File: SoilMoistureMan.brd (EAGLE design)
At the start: 23.5 x 69.9 mm, 22 parts, among them Q1 BC847CSMD, Q2 BC857C, Q3 BC847CSMD, Q4 BC847CSMD, Q5 BC847CSMD

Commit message: schematic and Routing changes
schematic and Routing changes still WIP
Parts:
- added BAT2: 2032, kzh20_lithium_batterie_holder:KZH20SMD
- D1: value SS12B -> S1A-13-F
- F1: value (none) -> Resettable_Fuse
- Q2: value BC857C -> BC847CSMD; device transistor:SOT23-BEC -> transistor-npn:SOT23
- Q3: value BC847CSMD -> BC857C; device transistor-npn:SOT23 -> transistor:SOT23-BEC
- R2: device resistor:R0805 -> rcl:R0805
- R3: value 1k -> 100k; device rcl:R0805 -> resistor:R0805
- R4: value 1k -> 10k
- R5: value 100k -> 1k
- R7: value 1k -> 100k
- moved R8 80.0 mm to (23.2, 62.2), turned to 270 degrees
- moved Q5 63.3 mm to (23.2, 51.4)
- moved D1 27.8 mm to (36.2, 40.6), turned to 180 degrees
- moved R4 19.1 mm to (17.6, 47.8), turned to 270 degrees
- moved F1 18.9 mm to (30.6, 37.3)
- moved Q4 16.8 mm to (5.08, 51.4), turned to 0 degrees
- moved Q3 16.3 mm to (21.0, 45.7)
- moved R6 9.53 mm to (9.21, 66.0), turned to 90 degrees
- moved R2 6.79 mm to (9.84, 49.2), turned to 270 degrees
- moved R7 5.85 mm to (18.7, 66.0), turned to 90 degrees
- moved Q1 5.82 mm to (6.19, 45.7)
- moved R5 5.62 mm to (5.08, 62.2)
- moved R3 3.49 mm to (16.5, 43.8)
- moved R1 3.34 mm to (11.6, 44.0)
- moved Q2 2.66 mm to (14.0, 47.5)
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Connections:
- new net N$13: Q2.3, R3.1, R4.1
- net GND: now also BAT2.-, Q2.2, Q5.2; no longer Q3.2
- net N$1: now also Q3.C, R8.2; no longer Q2.C, R4.2
- net N$10: now also Q4.1, R7.1; no longer Q3.1, R6.1
- net N$11: now also Q5.3; no longer Q4.3
- net N$12: now also Q5.1, R6.1; no longer Q4.1, R5.1
- net N$2: now also R5.1; no longer R4.1
- net N$3: now also Q3.B, R4.2; no longer Q2.B, R2.1, R3.2
- net N$4: now also Q2.1, R2.1; no longer R3.1
- net N$5: now also R8.1; no longer R7.1
- net N$6: now also Q3.E, R3.2; no longer Q2.E
- net N$7: now also Q4.3; no longer Q3.3
- net VCC: now also BAT2.+
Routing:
- net SOIL_PROBE_B: track 0.00 -> 114.4 mm, vias 0 -> 3
- net SOIL_PROBE_A: track 0.00 -> 71.2 mm, vias 0 -> 1
- net GND: track 0.00 -> 59.9 mm, vias 0 -> 6
- net N$1: track 0.00 -> 45.6 mm, vias 0 -> 2
- net VCC: track 0.00 -> 37.0 mm
- net N$10: track 0.00 -> 30.9 mm, vias 0 -> 2
- net N$12: track 0.00 -> 26.8 mm
- net N$6: track 0.00 -> 21.3 mm, vias 0 -> 3
- net N$4: track 0.00 -> 15.1 mm
- net N$13: track 0.00 -> 10.0 mm
- net N$5: track 0.00 -> 9.25 mm
- net N$11: track 0.00 -> 9.07 mm
- net N$7: track 0.00 -> 7.38 mm
- net N$3: track 0.00 -> 7.05 mm
- net N$2: track 0.00 -> 4.67 mm
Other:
- outline, holes or cut-outs redrawn

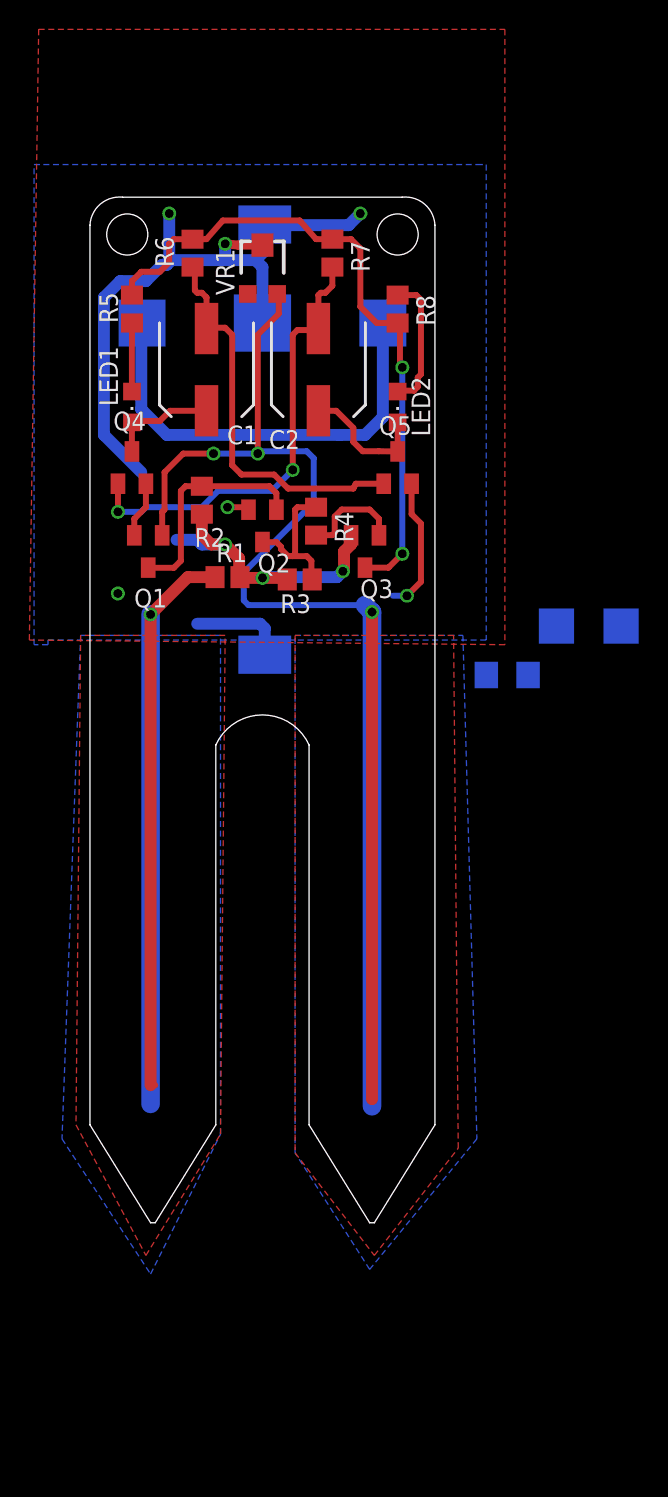
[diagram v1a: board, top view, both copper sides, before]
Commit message: Layout changes and Bat 2 changed to bat 1
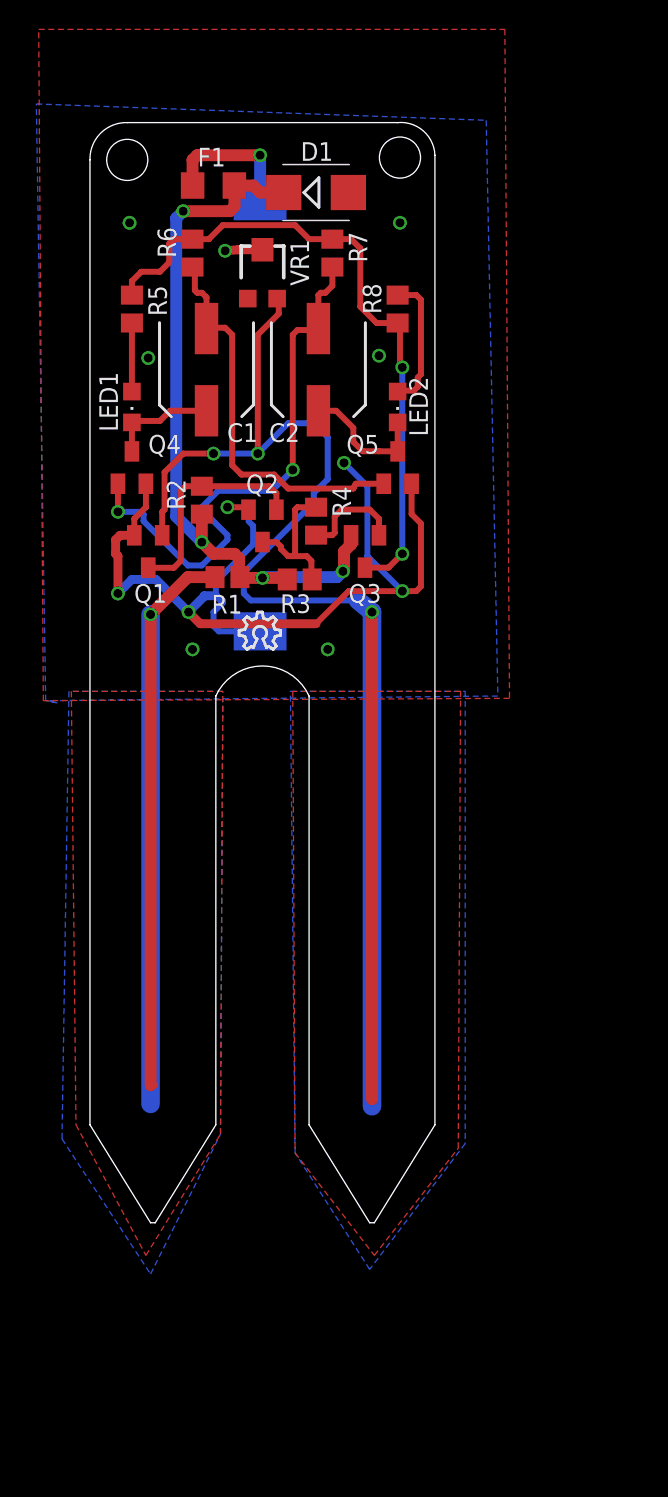
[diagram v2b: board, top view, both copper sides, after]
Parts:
- removed BAT2: 2032, kzh20_lithium_batterie_holder:KZH20SMD
- BAT1: value CR1220SMD -> 2032; device adafruit:CR1220-SMD -> kzh20_lithium_batterie_holder:KZH20SMD
- moved F1 38.9 mm to (10.6, 70.6), flipped to the top
- moved D1 34.9 mm to (17.6, 70.2), flipped to the top, turned to 0 degrees
- moved U$1 7.13 mm to (12.4, 39.1), flipped to the top
- moved BAT1 6.35 mm to (13.8, 54.9), turned to 90 degrees
- moved VR1 0.32 mm to (14.0, 64.8)
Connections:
- net GND: no longer BAT2.-
- net VCC: now also BAT1.+; no longer BAT1.+$1, BAT1.+$2, BAT2.+
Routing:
- net N$6: track 21.3 -> 50.2 mm, vias 3 -> 4
- net VCC: track 37.0 -> 9.61 mm, vias 0 -> 1
- net GND: track 59.9 -> 68.5 mm, vias 6 -> 12
- net N$10: track 30.9 -> 38.3 mm
- net SOIL_PROBE_B: track 114.4 -> 118.1 mm
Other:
- board size 23.5 x 69.9 mm -> 23.5 x 74.9 mm

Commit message: CAD B Commit
CAD B Commit - used to produce CAD B boards
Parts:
- removed Q5: BC847CSMD, transistor-npn:SOT23
- C1: value 100uF -> 1uF; device rcl:SANYO-OSCON_SMD_C6 -> resistor:C0603
- C2: value 10uF -> 100nF; device rcl:SANYO-OSCON_SMD_C6 -> resistor:C0603
- D1: value S1A-13-F -> 0.5A SOD-323; device diode:SMB -> adafruit:SOD-323F
- F1: value Resettable_Fuse -> 100MA PTC FUSE; device adafruit:R1206 -> rcl:R0805
- LED1, LED2: value GENERIC_0805_SMD_LED -> GENERIC_0603_SMD_LED; device led:CHIPLED_0805 -> led:SML0603
- Q2: value BC847CSMD -> BC857C; device transistor-npn:SOT23 -> transistor:SOT23-BEC
- Q3: value BC857C -> BC847CSMD; device transistor:SOT23-BEC -> transistor-npn:SOT23
- R1: value 20k -> 150k; device resistor:R0805 -> resistor:R0603
- R2: value 100k -> 1Meg; device rcl:R0805 -> resistor:R0603
- R3: value 100k -> 10k; device resistor:R0805 -> resistor:R0603
- R4: value 10k -> 1Meg; device rcl:R0805 -> resistor:R0603
- R5: value 1k -> 10Meg; device rcl:R0805 -> resistor:R0603
- R6: value 100k -> 10Meg; device rcl:R0805 -> resistor:R0603
- R7: value 100k -> 2k; device rcl:R0805 -> resistor:R0603
- R8: value 1k -> 0R0; device rcl:R0805 -> resistor:R0603
- moved D1 29.1 mm to (9.05, 42.4), flipped to the bottom, turned to 270 degrees
- moved F1 29.1 mm to (13.8, 41.8), flipped to the bottom
- moved R8 19.4 mm to (13.8, 45.2), turned to 0 degrees
- moved LED2 19.2 mm to (10.3, 69.8)
- moved LED1 18.8 mm to (17.3, 69.8), turned to 0 degrees
- moved Q1 16.2 mm to (22.1, 42.5), flipped to the bottom, turned to 0 degrees
- moved R6 16.1 mm to (15.2, 51.1)
- moved Q4 15.5 mm to (19.8, 46.7), flipped to the bottom
- moved R7 14.9 mm to (18.3, 51.1), turned to 270 degrees
- moved Q3 13.6 mm to (7.46, 47.0), flipped to the bottom, turned to 0 degrees
- moved R5 13.2 mm to (12.2, 51.1)
- moved C2 13.2 mm to (19.8, 45.1), turned to 0 degrees
- moved C1 13.0 mm to (7.46, 45.4), turned to 0 degrees
- moved R3 12.6 mm to (6.19, 51.1), turned to 270 degrees
- moved R2 11.7 mm to (21.4, 51.1), turned to 90 degrees
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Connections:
- removed net N$4: Q1.3, Q2.1, R2.1
- removed net N$6: D1.C, F1.2, Q3.E, R1.2, R2.2, R3.2
- removed net SOIL_PROBE_B: Q1.1, VR1.3
- new net N$9: R1.2, VR1.2
- new net VCC_FUSED: D1.C, F1.2, Q2.E, R2.2, VR1.3
- net GND: now also Q3.2; no longer Q2.2, Q5.2, VR1.2
- net N$1: now also Q2.C, R4.2; no longer Q3.C, R8.2
- net N$10: now also C2.1, Q3.1, R6.1; no longer C2.-, Q4.1, R7.1
- net N$11: now also C2.2, LED1.C, Q4.3; no longer C2.+, Q5.3
- net N$12: now also C1.2, Q4.1, R5.1; no longer C1.-, Q5.1, R6.1
- net N$13: now also Q1.3, R2.1; no longer Q2.3, R4.1
- net N$2: now also R4.1, R8.2; no longer LED1.A, R5.1
- net N$3: now also Q2.B, R3.2; no longer Q3.B, R4.2
- net N$5: now also LED1.A, R7.1; no longer R8.1
- net N$7: now also C1.1, Q3.3, R8.1; no longer C1.+, LED1.C, Q4.3
- net SOIL_PROBE_A: now also Q1.1
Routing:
- net SOIL_PROBE_B: track 118.1 -> 0.00 mm, vias 3 -> 0
- net VCC_FUSED: track 0.00 -> 92.0 mm, vias 0 -> 1
- net N$6: track 50.2 -> 0.00 mm, vias 4 -> 0
- net SOIL_PROBE_A: track 71.2 -> 21.0 mm, vias 1 -> 4
- net N$9: track 0.00 -> 36.1 mm, vias 0 -> 3
- net N$11: track 9.07 -> 40.8 mm, vias 0 -> 4
- net N$5: track 9.25 -> 33.0 mm, vias 0 -> 4
- net N$10: track 38.3 -> 15.5 mm, vias 2 -> 1
- net GND: track 68.5 -> 91.0 mm, vias 12 -> 17
- net N$13: track 10.0 -> 29.2 mm, vias 0 -> 1
- net N$4: track 15.1 -> 0.00 mm
- net N$1: track 45.2 -> 33.3 mm
- net N$2: track 4.67 -> 13.5 mm
- net N$3: track 7.05 -> 15.5 mm, vias 0 -> 1
- net N$7: track 7.38 -> 13.6 mm, vias 0 -> 1
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- removed copper zone on layer 1, net SOIL_PROBE_B
- removed copper zone on layer 16, net SOIL_PROBE_B
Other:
- board size 23.5 x 74.9 mm -> 23.5 x 77.5 mm
- board text added: "K"

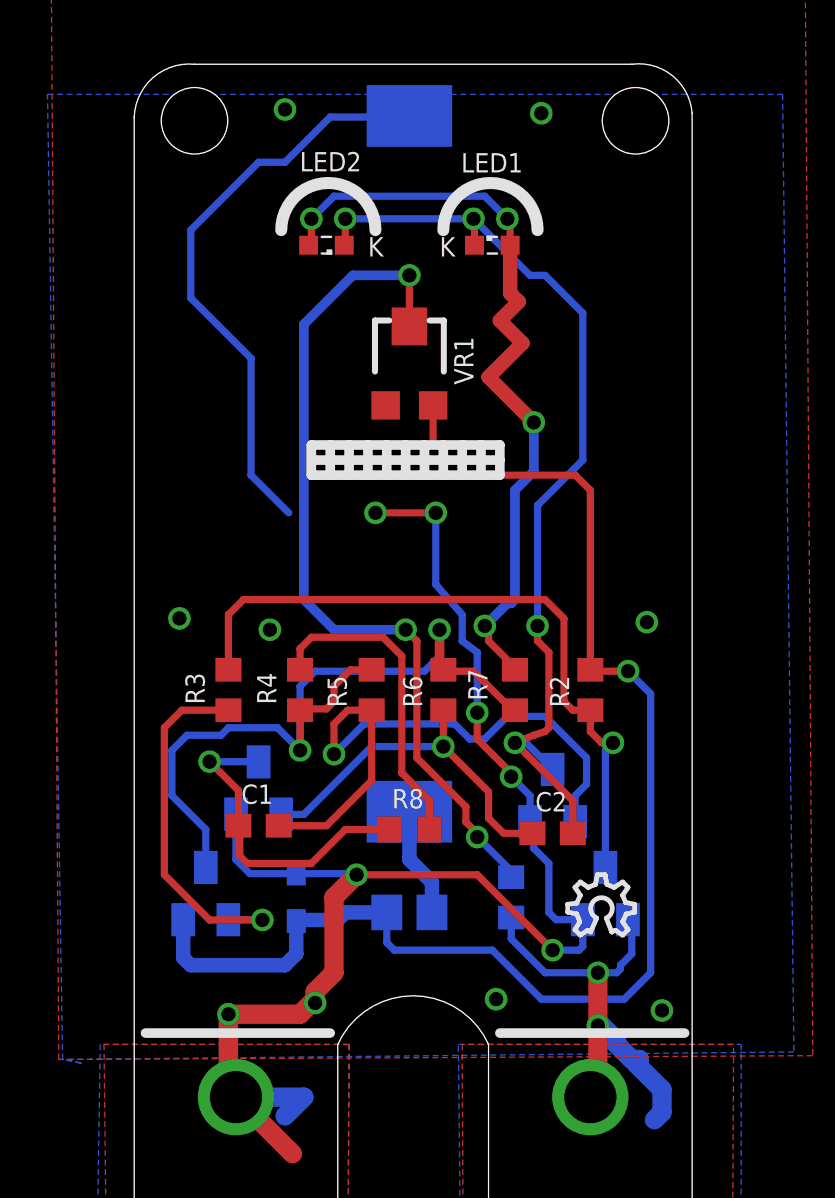
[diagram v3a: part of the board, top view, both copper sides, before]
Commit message: First CAD C commit
Updated one resistor value from 1MOhm to 100k. added warning text about
electrolysis to pcb and another to the schematic
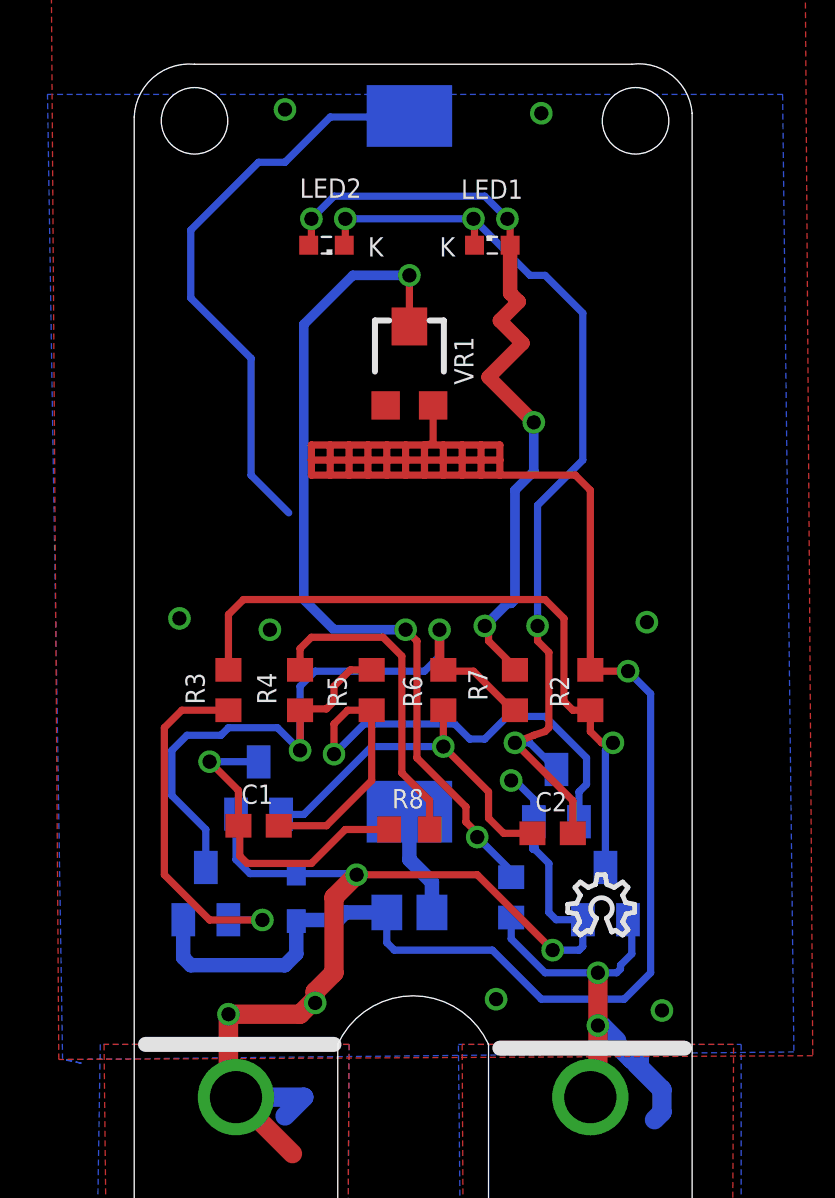
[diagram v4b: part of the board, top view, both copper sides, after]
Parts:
- Q4: value BC847CSMD -> MMBTA13LT1; device transistor-npn:SOT23 -> transistor-npn:SOT23-BEC
- R4: value 1Meg -> 100k
- moved Q4 0.16 mm to (20.0, 46.7)
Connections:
- net GND: now also Q4.E; no longer Q4.2
- net N$11: now also Q4.C; no longer Q4.3
- net N$12: now also Q4.B; no longer Q4.1
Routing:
- net GND: track 91.0 -> 76.0 mm, vias 17 -> 14
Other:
- board text added: "CAD C"
- board text added: "WARNING: DUE TO ELECTROLYSIS - DO NOT USE ON EDIBLE PLANTS !!!"
- board text removed: "CAD B"

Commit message: Committing latest updates on CAD C
Committing latest updates on CAD C
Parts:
- LED1, LED2: value GENERIC_0603_SMD_LED -> GREEN LED; device led:SML0603 -> P-LCC-2_Shorter:P-LCC-2
- R7: value 2k -> 560R
- VR1: device adafruit:TC33X -> P-LCC-2_Shorter:TC33X
- moved LED1 0.22 mm to (17.1, 70.0), turned to 270 degrees
- moved LED2 0.16 mm to (10.3, 70.0), turned to 90 degrees
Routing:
- net GND: track 76.0 -> 102.9 mm, vias 14 -> 18
- net SOIL_PROBE_A: track 21.0 -> 29.4 mm, vias 4 -> 3
- net N$5: track 33.0 -> 37.1 mm
- net N$11: track 41.0 -> 43.1 mm
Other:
- board size 23.5 x 77.5 mm -> 23.5 x 89.4 mm
